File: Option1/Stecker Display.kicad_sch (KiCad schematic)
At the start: 0 parts

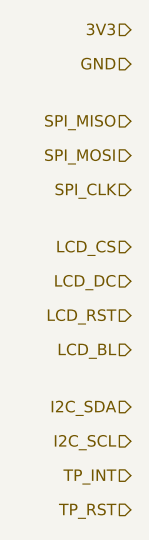
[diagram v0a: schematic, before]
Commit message: SPI Flash hinzugefügt, IN/Outputs vereinheitlicht, USB Flash Möglichkeit hinzugefügt, Display fehtl noch
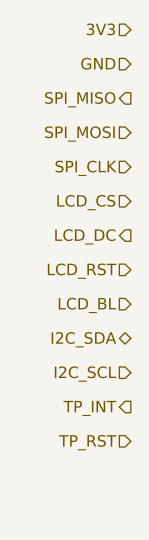
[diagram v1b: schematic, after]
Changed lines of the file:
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@@
 (kicad_sch
-	(version 20231120)
+	(version 20250114)
 	(generator "eeschema")
-	(generator_version "8.0")
+	(generator_version "9.0")
 	(paper "A4")
 	(title_block
@@
 		(comment 3 "Sebastian Hampl")
 	)
+	(hierarchical_label "TP_INT"
+		(shape output)
+		(at 38.1 64.77 180)
+		(effects
+			(font
+				(size 1.27 1.27)
+			)
+			(justify right)
+		)
+	)
 	(hierarchical_label "LCD_CS"
 		(shape input)
-		(at 38.1 46.99 180)
+		(at 38.1 41.91 180)
+		(effects
+			(font
+				(size 1.27 1.27)
+			)
+			(justify right)
+		)
+	)
+	(hierarchical_label "LCD_DC"
+		(shape output)
+		(at 38.1 45.72 180)
 		(effects
 			(font
@@
 		)
 	)
-	(hierarchical_label "TP_INT"
+	(hierarchical_label "SPI_CLK"
 		(shape input)
-		(at 38.1 72.39 180)
+		(at 38.1 38.1 180)
 		(effects
 			(font
@@
 		)
 	)
-	(hierarchical_label "SPI_CLK"
-		(shape input)
-		(at 38.1 40.64 180)
+	(hierarchical_label "I2C_SDA"
+		(shape bidirectional)
+		(at 38.1 57.15 180)
 		(effects
 			(font
@@
 	(hierarchical_label "LCD_RST"
 		(shape input)
-		(at 38.1 54.61 180)
-		(effects
-			(font
-				(size 1.27 1.27)
-			)
-			(justify right)
-		)
-	)
-	(hierarchical_label "SPI_MISO"
-		(shape input)
-		(at 38.1 33.02 180)
+		(at 38.1 49.53 180)
 		(effects
 			(font
@@
 	(hierarchical_label "SPI_MOSI"
 		(shape input)
-		(at 38.1 36.83 180)
+		(at 38.1 34.29 180)
 		(effects
 			(font
@@
 	(hierarchical_label "I2C_SCL"
 		(shape input)
-		(at 38.1 68.58 180)
+		(at 38.1 60.96 180)
 		(effects
 			(font
@@
 	(hierarchical_label "LCD_BL"
 		(shape input)
-		(at 38.1 58.42 180)
+		(at 38.1 53.34 180)
 		(effects
 			(font
@@
 	(hierarchical_label "TP_RST"
 		(shape input)
-		(at 38.1 76.2 180)
+		(at 38.1 68.58 180)
 		(effects
 			(font
@@
 		)
 	)
-	(hierarchical_label "LCD_DC"
-		(shape input)
-		(at 38.1 50.8 180)
+	(hierarchical_label "SPI_MISO"
+		(shape output)
+		(at 38.1 30.48 180)
 		(effects
 			(font
-				(size 1.27 1.27)
-			)
-			(justify right)
-		)
-	)
-	(hierarchical_label "I2C_SDA"
-		(shape input)
-		(at 38.1 64.77 180)
-		(effects
-			(font

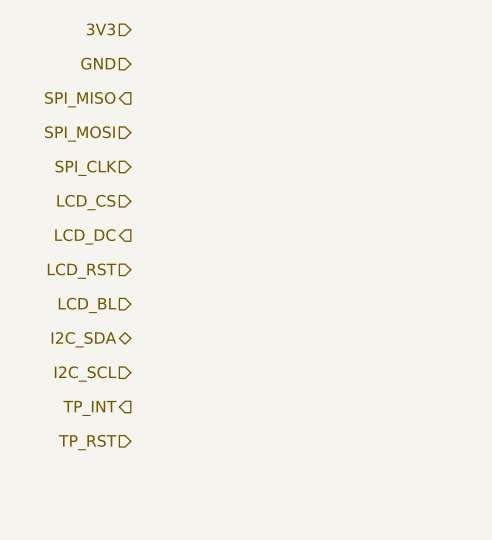
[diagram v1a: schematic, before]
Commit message: MCT und SPI zu Layout hinzugefügt
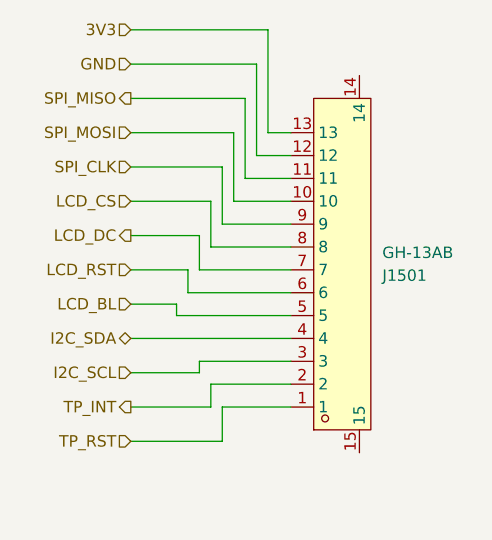
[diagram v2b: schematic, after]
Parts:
- added J1501: GH-13AB, easyeda2kicad:CONN-SMD_GH-13AB, symbol easyeda2kicad:GH-13AB
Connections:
- net 3V3: now also J1501.13
- net GND: now also J1501.12
- net I2C_SCL: now also J1501.3
- net I2C_SDA: now also J1501.4
- net LCD_BL: now also J1501.5
- net LCD_CS: now also J1501.8
- net LCD_DC: now also J1501.7
- net LCD_RST: now also J1501.6
- net SPI_CLK: now also J1501.9
- net SPI_MISO: now also J1501.11
- net SPI_MOSI: now also J1501.10
- net TP_INT: now also J1501.2
- net TP_RST: now also J1501.1

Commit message: Platine korrigeiert, 5V DCDC getauscht, 3.3V Display Versorgung entfernt. Bauteile neu angeordnet, USB 5V auf 5V Supply geführt
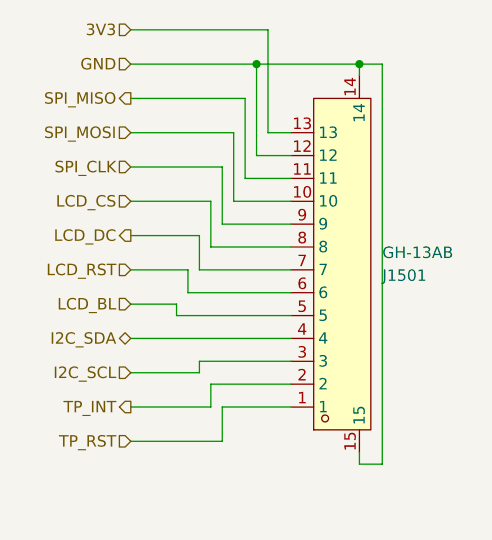
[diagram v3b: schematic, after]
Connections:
- net GND: now also J1501.14, J1501.15
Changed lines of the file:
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@@
 		(comment 3 "Sebastian Hampl")
 	)
+	(junction
+		(at 52.07 26.67)
+		(diameter 0)
+		(color 0 0 0 0)
+	)
+	(junction
+		(at 63.5 26.67)
+		(diameter 0)
+		(color 0 0 0 0)
+	)
 	(wire
 		(pts
@@
 	(wire
 		(pts
+			(xy 53.34 34.29) (xy 55.88 34.29)
+		)
+		(stroke
+			(width 0)
+			(type default)
+		)
+	)
+	(wire
+		(pts
 			(xy 48.26 44.45) (xy 48.26 38.1)
 		)
@@
 	(wire
 		(pts
+			(xy 63.5 27.94) (xy 63.5 26.67)
+		)
+		(stroke
+			(width 0)
+			(type default)
+		)
+	)
+	(wire
+		(pts
 			(xy 45.72 49.53) (xy 55.88 49.53)
 		)
@@
 	(wire
 		(pts
+			(xy 63.5 71.12) (xy 63.5 69.85)
+		)
+		(stroke
+			(width 0)
+			(type default)
+		)
+	)
+	(wire
+		(pts
 			(xy 52.07 26.67) (xy 52.07 36.83)
 		)
@@
 	(wire
 		(pts
-			(xy 53.34 34.29) (xy 55.88 34.29)
-		)
-		(stroke
-			(width 0)
-			(type default)
-		)
-	)
-	(wire
-		(pts
 			(xy 46.99 41.91) (xy 46.99 46.99)
 		)
@@
 	(wire
 		(pts
+			(xy 66.04 26.67) (xy 63.5 26.67)
+		)
+		(stroke
+			(width 0)
+			(type default)
+		)
+	)
+	(wire
+		(pts
 			(xy 55.88 54.61) (xy 43.18 54.61)
 		)
@@
 	(wire
 		(pts
+			(xy 52.07 26.67) (xy 63.5 26.67)
+		)
+		(stroke
+			(width 0)
+			(type default)
+		)
+	)
+	(wire
+		(pts
 			(xy 38.1 22.86) (xy 53.34 22.86)
 		)
 		(stroke
+			(width 0)
+			(type default)
+		)
+	)
+	(wire
+		(pts
+			(xy 63.5 71.12) (xy 66.04 71.12)
+		)
+		(stroke
+			(width 0)
+			(type default)
+		)
+	)
+	(wire
+		(pts
+			(xy 66.04 26.67) (xy 66.04 71.12)
+		)
+		(stroke
